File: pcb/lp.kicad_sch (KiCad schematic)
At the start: 7 parts, among them J41 Conn_01x02_Pin, Q2 IRLML0030

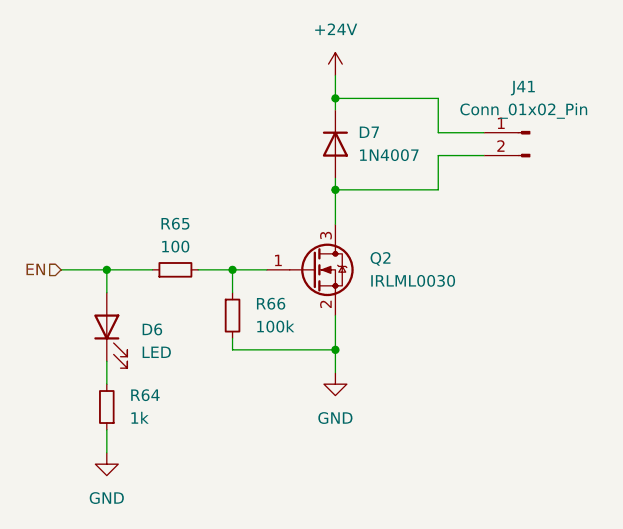
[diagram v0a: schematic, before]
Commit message: fixes #8: changed led series resistor values
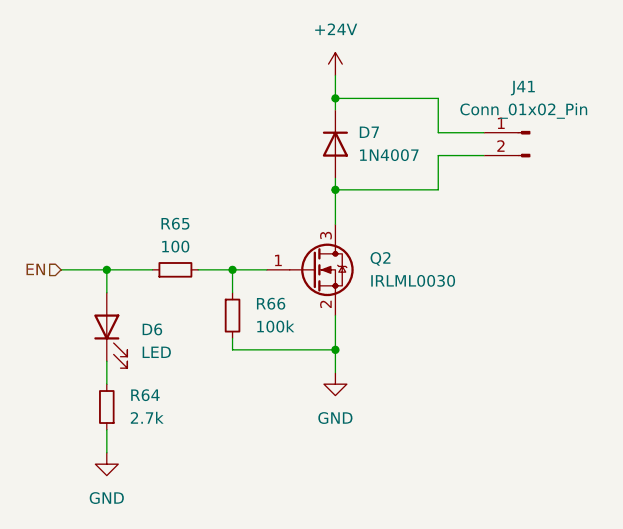
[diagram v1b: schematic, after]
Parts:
- R64: value 1k -> 2.7k
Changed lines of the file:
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@@
 		(fields_autoplaced yes)
 		(property "Reference" "R64"
-			(at 36.83 57.15 0)
+			(at 36.83 57.1499 0)
 			(effects
 				(font
@@
 			)
 		)
-		(property "Value" "1k"
-			(at 36.83 59.69 0)
+		(property "Value" "2.7k"
+			(at 36.83 59.6899 0)
 			(effects
 				(font

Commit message: fixes #6
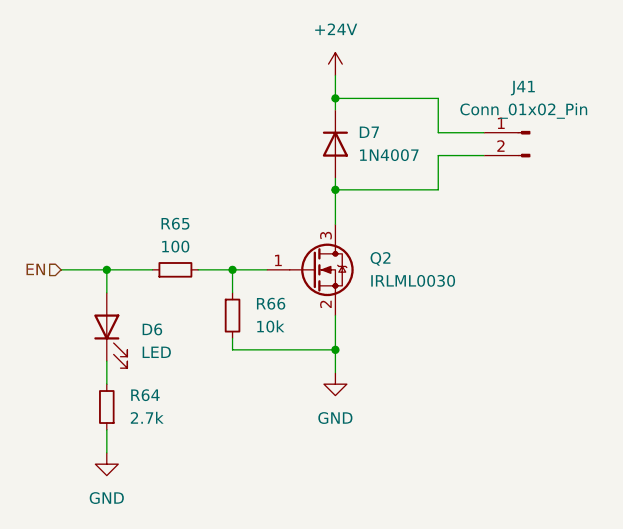
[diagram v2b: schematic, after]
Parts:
- R66: value 100k -> 10k
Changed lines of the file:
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@@
 		(fields_autoplaced yes)
 		(property "Reference" "R66"
-			(at 50.8 46.99 0)
+			(at 50.8 46.9899 0)
 			(effects
 				(font
@@
 			)
 		)
-		(property "Value" "100k"
-			(at 50.8 49.53 0)
+		(property "Value" "10k"
+			(at 50.8 49.5299 0)
 			(effects
 				(font

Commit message: specified some values and colors added lcsc part ids for all components
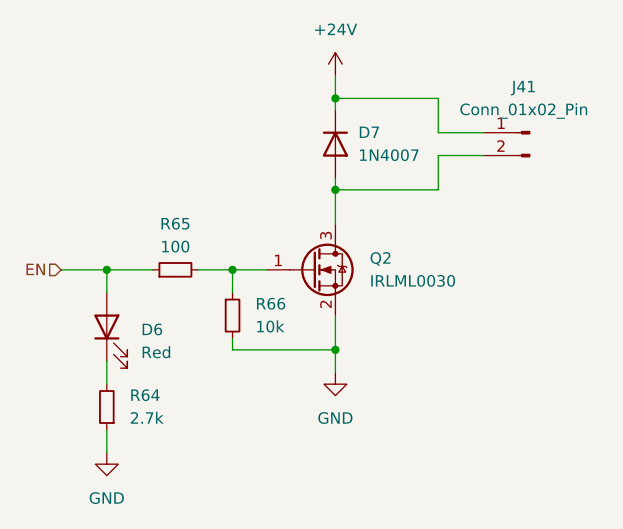
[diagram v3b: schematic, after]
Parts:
- D6: value LED -> Red; LCSC (none) -> C965799
- D7: LCSC (none) -> C2902912
- J41: LCSC (none) -> C378939
- Q2: LCSC (none) -> C67272
- R64: LCSC (none) -> C13167
- R65: LCSC (none) -> C105588
- R66: LCSC (none) -> C98220
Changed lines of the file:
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@@
+			)
+		)
+		(property "LCSC" "C98220"
+			(at 50.8 46.9899 0)
+			(effects
+				(font
+					(size 1.27 1.27)
+				)
+				(hide yes)
 			)
 		)
@@
 			)
 		)
+		(property "LCSC" "C13167"
+			(at 36.83 57.1499 0)
+			(effects
+				(font
+					(size 1.27 1.27)
+				)
+				(hide yes)
+			)
+		)
 		(pin "1"
 		)
@@
 		(fields_autoplaced yes)
 		(property "Reference" "D6"
-			(at 38.1 49.8475 90)
+			(at 38.1 49.8474 90)
 			(effects
 				(font
@@
 			)
 		)
-		(property "Value" "LED"
-			(at 38.1 52.3875 90)
+		(property "Value" "Red"
+			(at 38.1 52.3874 90)
 			(effects
 				(font
@@
 		(property "Description" "Light emitting diode"
 			(at 34.29 49.53 0)
+			(effects
+				(font
+					(size 1.27 1.27)
+				)
+				(hide yes)
+			)
+		)
+		(property "LCSC" "C965799"
+			(at 38.1 49.8474 0)
 			(effects
 				(font
@@
 			)
 		)
+		(property "LCSC" "C67272"
+			(at 63.5 41.91 0)
+			(effects
+				(font
+					(size 1.27 1.27)
+				)
+				(hide yes)
+			)
+		)
 		(pin "2"
 		)
@@
 			)
 		)
+		(property "LCSC" "C105588"
+			(at 41.91 38.1 0)
+			(effects
+				(font
+					(size 1.27 1.27)
+				)
+				(hide yes)
+			)
+		)
 		(pin "1"
 		)
@@
 			)
 		)
+		(property "LCSC" "C2902912"
+			(at 62.23 27.94 0)
+			(effects
+				(font
+					(size 1.27 1.27)
+				)
+				(hide yes)
+			)
+		)
 		(pin "1"
 		)
@@
 			(effects
 				(font
+					(size 1.27 1.27)
+				)
+				(hide yes)
+			)
+		)
+		(property "LCSC" "C378939"
+			(at 80.645 22.86 0)
+			(effects
+				(font
